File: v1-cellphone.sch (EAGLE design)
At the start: 96 parts, among them J1 AVRISP, J2 ZX62D-B-5P8, J3 PA, J4 PB, J5 PC, J8 FTDI, J9 BATTERY INPUT, Q1 MIC, Q2 NTR4501N-D, Q3 NTR4501N-D, U1 MCP73831, U2 MEGA1284, U3 GSM_UC15, U4 TXB0104PWR, X1 BU-SMA-V, X2 16MHz, X3 CCM03-3002 R102

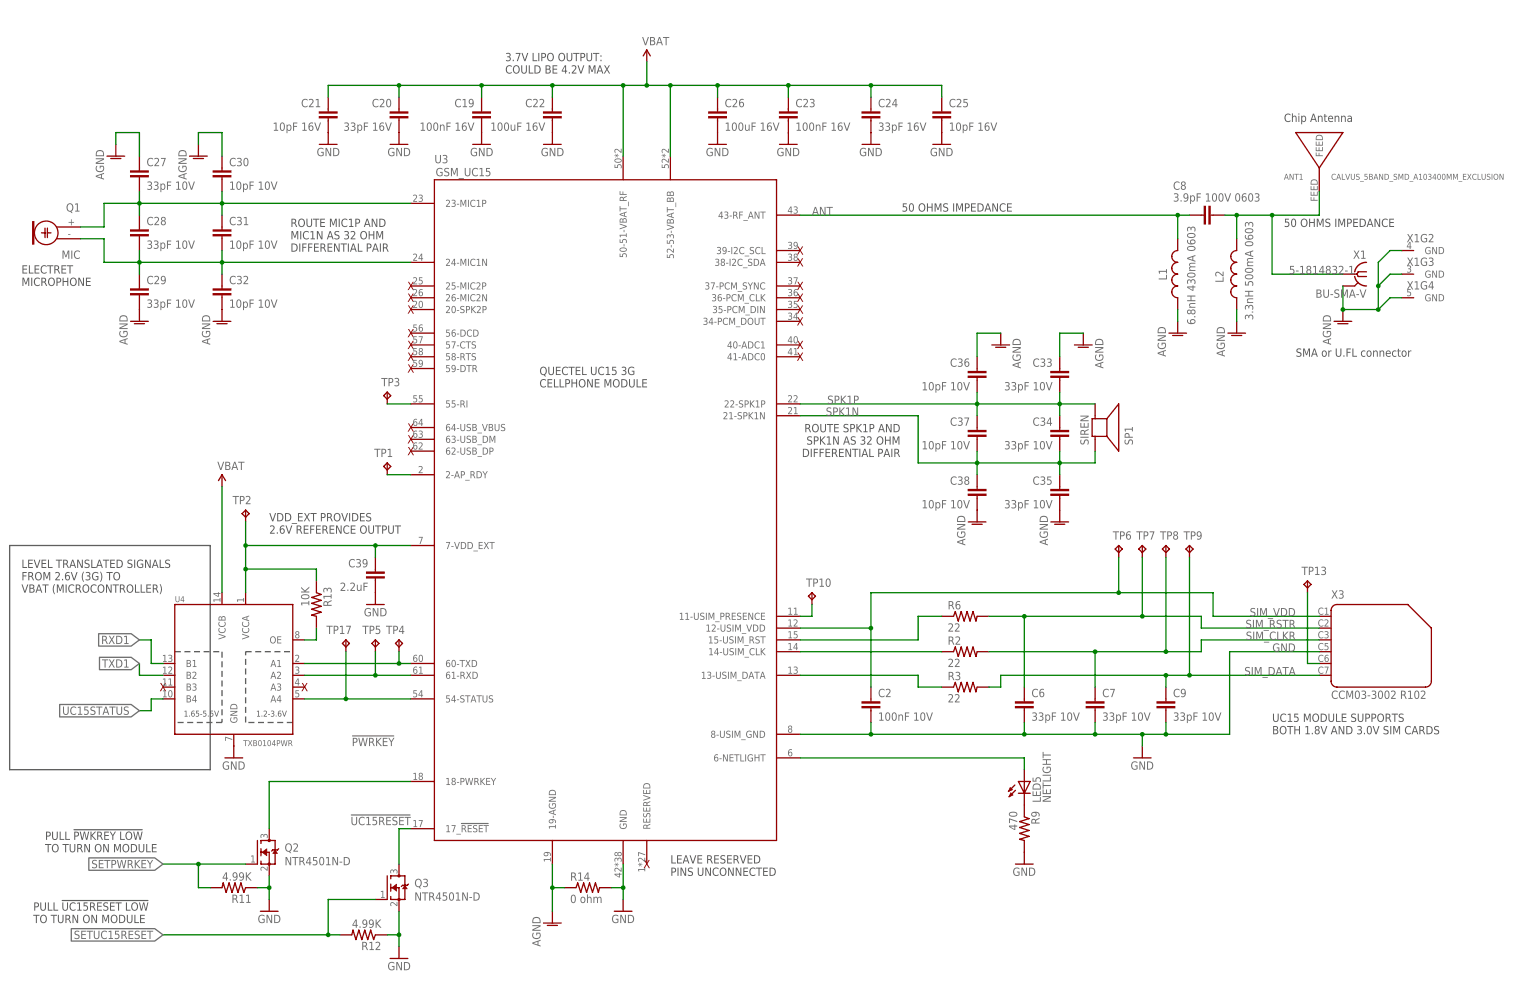
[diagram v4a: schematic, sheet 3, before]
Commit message: Added caps, made frames same size.
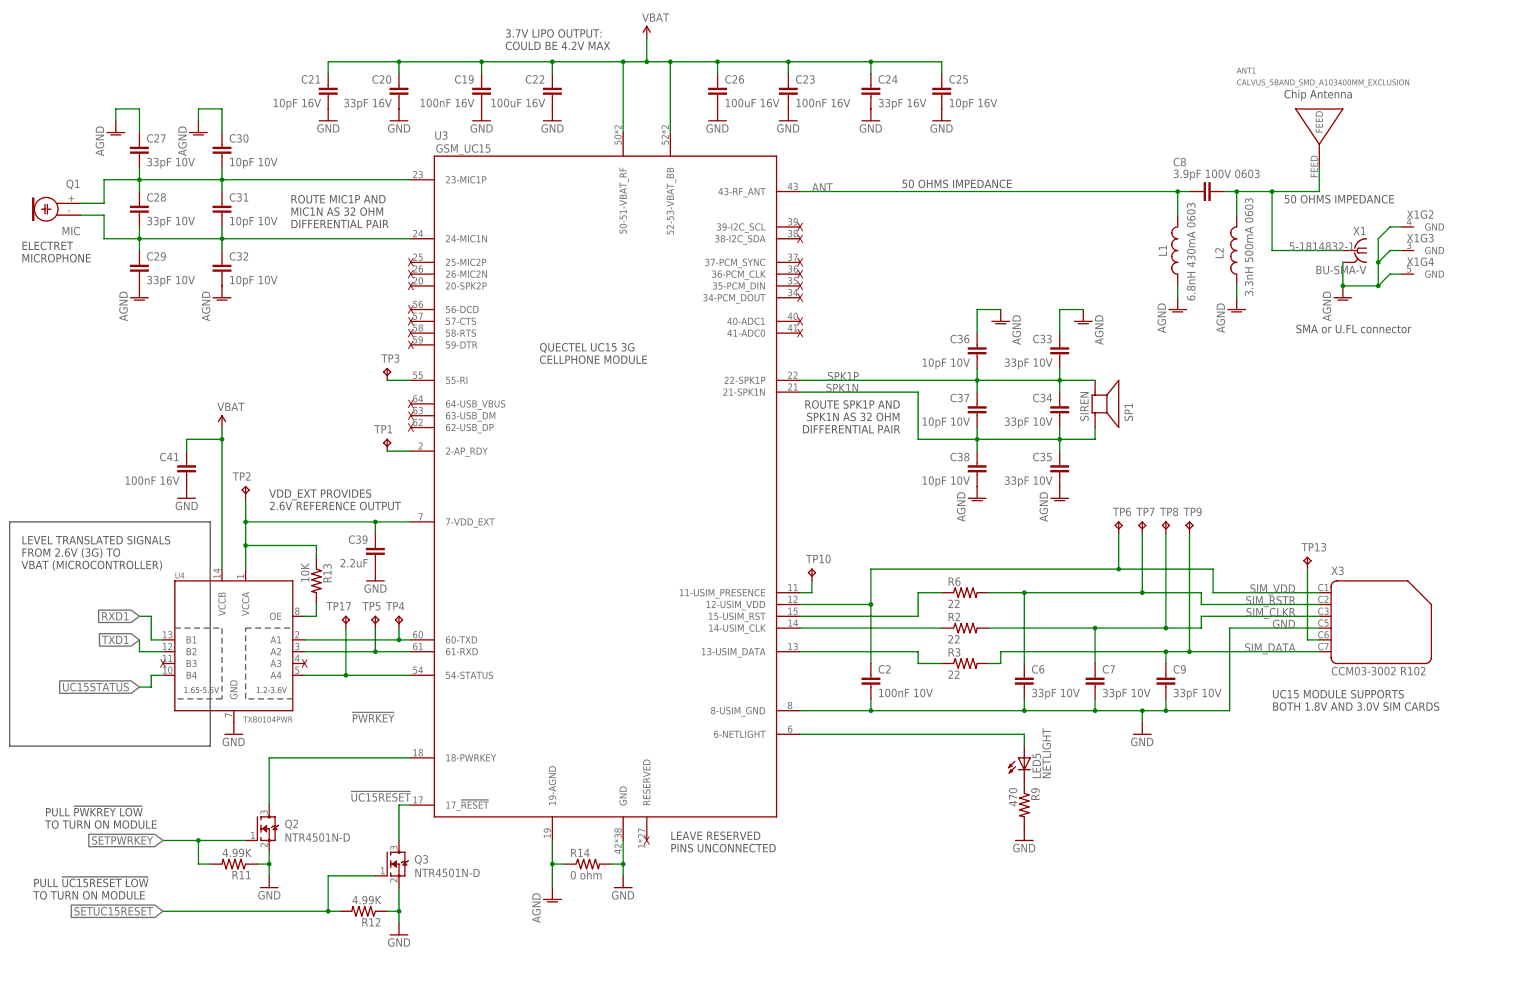
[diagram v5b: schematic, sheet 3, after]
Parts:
- added C40: 10nF 16V, rcl_custom:C-EU0603-B
- added C41: 100nF 16V, rcl_custom:C-EU0603-B
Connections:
- net !RESET: now also C40.1
- net GND: now also C40.2, C41.2
- net VBAT: now also C41.1
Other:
- note added: "INPUT MICRO USB FOR VOLTAGE TO CHARGE BATTERY"
- note added: "RESET SWITCH DEBOUNCE"
- note removed: "ATMEGA1284 MICROCONTROLLER"
- note removed: "INPUT MICRO USB FOR VOLTAGE OFF BATTERY"
- moved on the sheet: ANT1, C1, C10, C12, C14, C15, C17, C18, C19, C2, C20, C21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

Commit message: Verified packages. Minor tweaks throughout.
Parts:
- removed C16: 1mF 50V, cellphone-rcl:CPOL-USD/7343-31R
- removed J8: FTDI, cellphone:ARDUINO_SERIAL_PROGRAMSMD-NOHOLES
- removed J9: BATTERY INPUT, SparkFun-Connectors:M02-JST-2MM-SMT
- C11: device cellphone-rcl:CPOL-USD/7343-31R -> SparkFun-Capacitors:CAP_POLPTH4
- C2: value 100nF 10V -> 100nF 16V
- C27, C28, C29, C33, C35, C6, C7, C9: value 33pF 10V -> 33pF 16V
- C30: value 10pF 10V -> 10pF 10V
- C31, C32, C36, C37, C38: value 10pF 10V -> 10pF 16V
- C39: value 2.2uF -> 4.7uF 16V
- C4: value 4.7uF -> 4.7uF 16V
- J3: value PA -> GPIO; device SparkFun-Connectors:M08LOCK_LONGPADS -> SparkFun-Connectors:M20LOCK_LONGPADS
- J4: value PB -> FTDI; device SparkFun-Connectors:M04LOCK_LONGPADS -> SparkFun-Connectors:ARDUINO_SERIAL_PROGRAMLOCK
- J5: value PC -> BATTERY INPUT; device SparkFun-Connectors:M08LOCK_LONGPADS -> SparkFun-Connectors:M02-JST-2MM-SMT
- SP1: value SIREN -> SPEAKER
- X1: value BU-SMA-V -> SMA; device con-coax:BU-SMA-V -> v1-cellphone:CON-COAX_BU-SMA-V
- X2: value 16MHz -> 8MHz
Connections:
- net 5V: now also J4.VCC; no longer J8.VCC
- net GND: now also J4.CTS, J4.GND, J5.1; no longer C16.-, J8.GND, J9.1
- net N$5: now also J4.DTR; no longer J8.DTR
- net PB0: now also J3.9; no longer J4.1
- net PB1: now also J3.10; no longer J4.2
- net PB2: now also J3.11; no longer J4.3
- net PB3: now also J3.12; no longer J4.4
- net PC0: now also J3.13; no longer J5.1
- net PC1: now also J3.14; no longer J5.2
- net PC2: now also J3.15; no longer J5.3
- net PC3: now also J3.16; no longer J5.4
- net PC4: now also J3.17; no longer J5.5
- net PC5: now also J3.18; no longer J5.6
- net PC6: now also J3.19; no longer J5.7
- net PC7: now also J3.20; no longer J5.8
- net RXD0: now also J4.TXO; no longer J8.TXO
- net SPK1N: now also SP1.NEG; no longer SP1.1
- net SPK1P: now also SP1.POS; no longer SP1.2
- net TXD0: now also J4.RXI; no longer J8.RXI
- net VBAT: now also J5.2; no longer C16.+, J9.2
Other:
- note added: "TODO MAKE BOM PUT FRAMES ON SCHEMATIC MAKE CELLPHONE LIBRARY OF PACKAGES LAY OUT THE BOARD WRITE EVERYTHING UP REVIEW BOARD POST ON THE WEB"
- note removed: "TODO MAKE CELLPHONE LIBRARY OF PACKAGES LAY OUT THE BOARD MAKE BOM WRITE EVERYTHING UP REVIEW BOARD POST ON THE WEB"
- moved on the sheet: C13, C39, LED5, R9, SP1

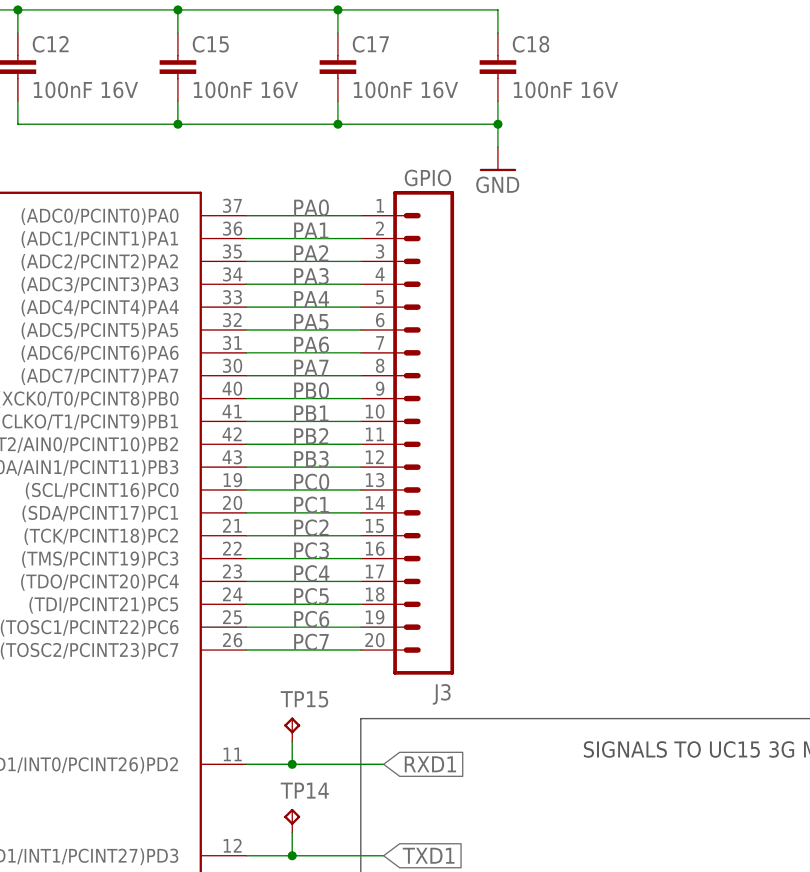
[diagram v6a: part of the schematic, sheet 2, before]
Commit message: All tracks routed. Needs review and impedance checks.
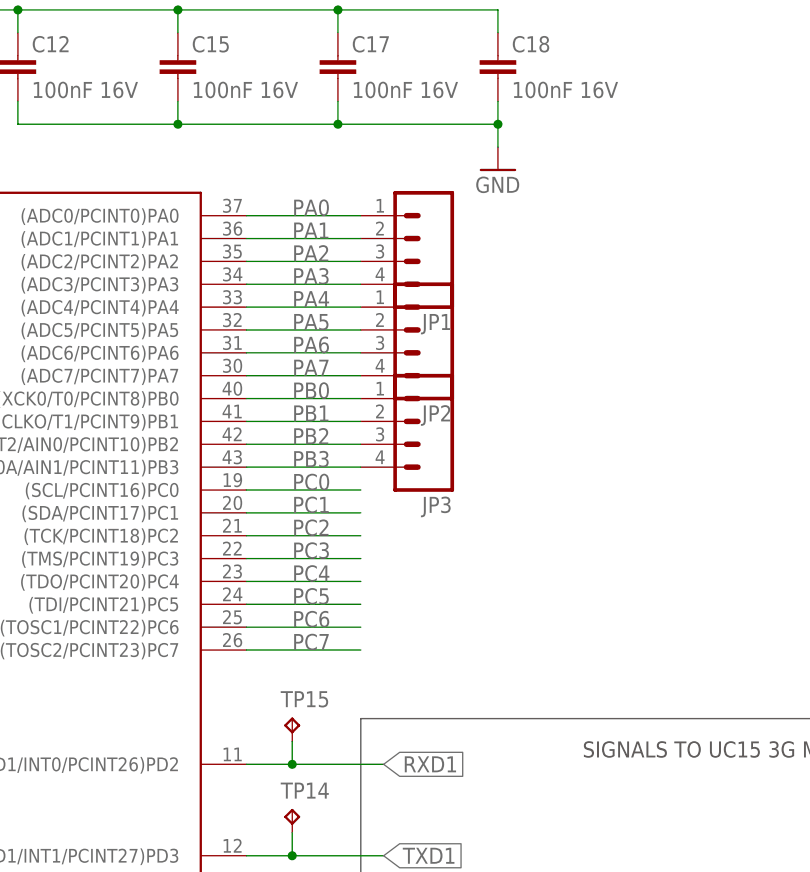
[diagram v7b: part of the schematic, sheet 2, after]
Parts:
- removed J3: GPIO, SparkFun-Connectors:M20LOCK_LONGPADS
- removed TP17, TP2, TP4, TP5: TPPAD1-13, testpad:TPPAD1-13
- added JP1, JP2, JP3: (no value), SparkFun-Connectors:M04LOCK
- C22, C26: device rcl_custom:C-EU0603-B -> rcl_custom:C-EUC1210K
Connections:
- net N$10 renamed PRESENCE
- net N$14 renamed OE
- net N$16 renamed MIC1P
- net N$19 renamed MIC1N
- net N$7 renamed XTAL2
- net N$8 renamed XTAL1
- net PB4 renamed DEBUGLED
- removed net 2.6V: C39.1, R13.1, TP2.TP, U3.7-VDD_EXT, U4.VCCA
- new net VDD_EXT: C39.1, R13.1, U3.7-VDD_EXT, U4.VCCA
- net N$20: no longer TP4.TP
- net N$21: no longer TP5.TP
- net N$23: no longer TP17.TP
- net PA0: now also JP1.1; no longer J3.1
- net PA1: now also JP1.2; no longer J3.2
- net PA2: now also JP1.3; no longer J3.3
- net PA3: now also JP1.4; no longer J3.4
- net PA4: now also JP2.1; no longer J3.5
- net PA5: now also JP2.2; no longer J3.6
- net PA6: now also JP2.3; no longer J3.7
- net PA7: now also JP2.4; no longer J3.8
- net PB0: now also JP3.1; no longer J3.9
- net PB1: now also JP3.2; no longer J3.10
- net PB2: now also JP3.3; no longer J3.11
- net PB3: now also JP3.4; no longer J3.12
- net PC0: no longer J3.13
- net PC1: no longer J3.14
- net PC2: no longer J3.15
- net PC3: no longer J3.16
- net PC4: no longer J3.17
- net PC5: no longer J3.18
- net PC6: no longer J3.19
- net PC7: no longer J3.20
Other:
- note added: "CELLPHONE3G PROTOTYPING MODULE VERSION 1.3 8/8/2014"
- note removed: "CELLPHONE3G PROTOTYPING MODULE VERSION 1.2 8/2/2014"
- note removed: "TODO MAKE BOM PUT FRAMES ON SCHEMATIC MAKE CELLPHONE LIBRARY OF PACKAGES LAY OUT THE BOARD WRITE EVERYTHING UP REVIEW BOARD POST ON THE WEB"
- moved on the sheet: TP13
